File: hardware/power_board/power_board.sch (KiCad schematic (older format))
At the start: 25 parts, among them J1 Barrel_Jack, J2 Conn_01x05_Male, U1 LM1117-ADJ, U2 LM1117-ADJ, U3 LM1117-ADJ, U4 LM2776

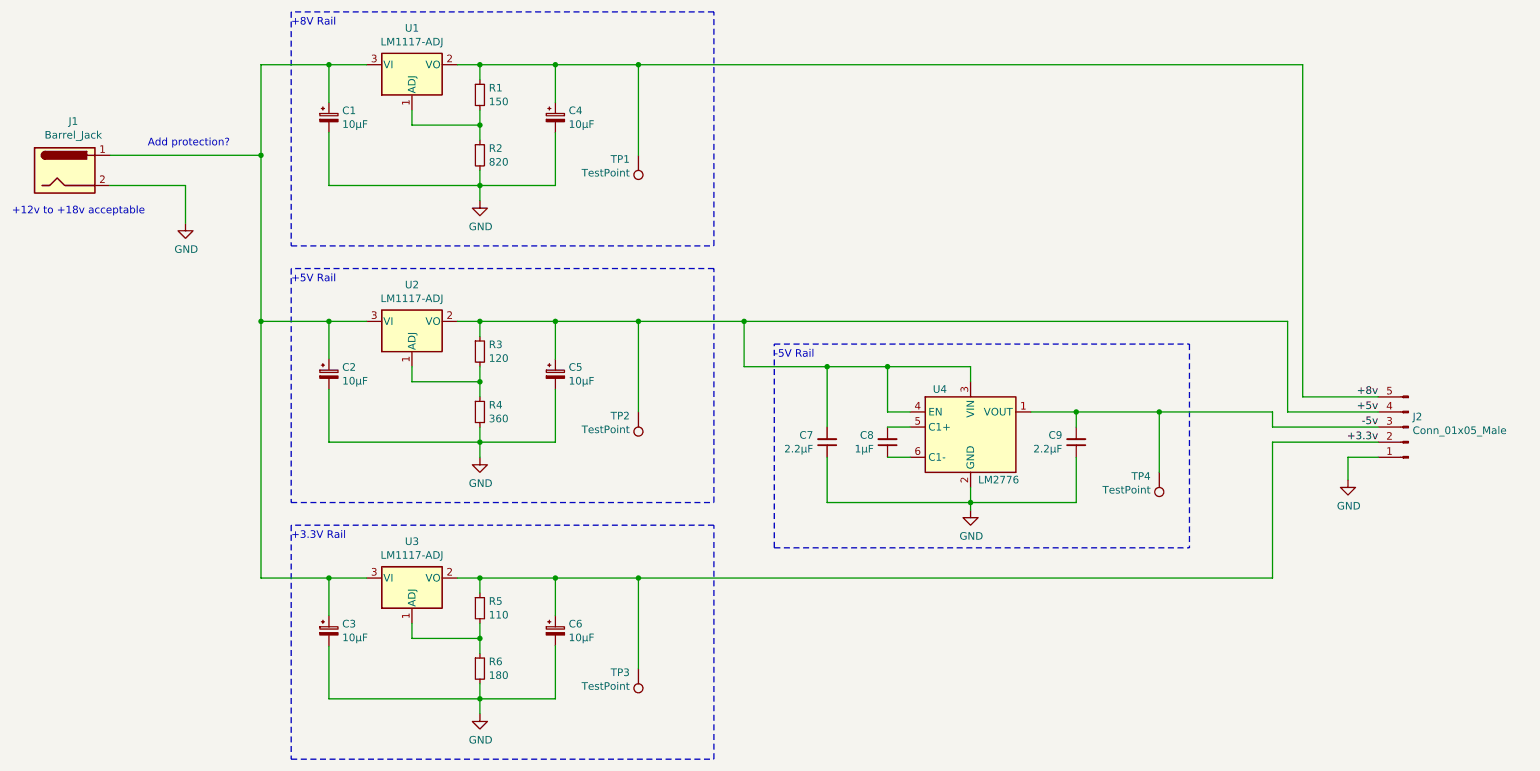
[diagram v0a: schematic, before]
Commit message: Made the board design a little more spacious
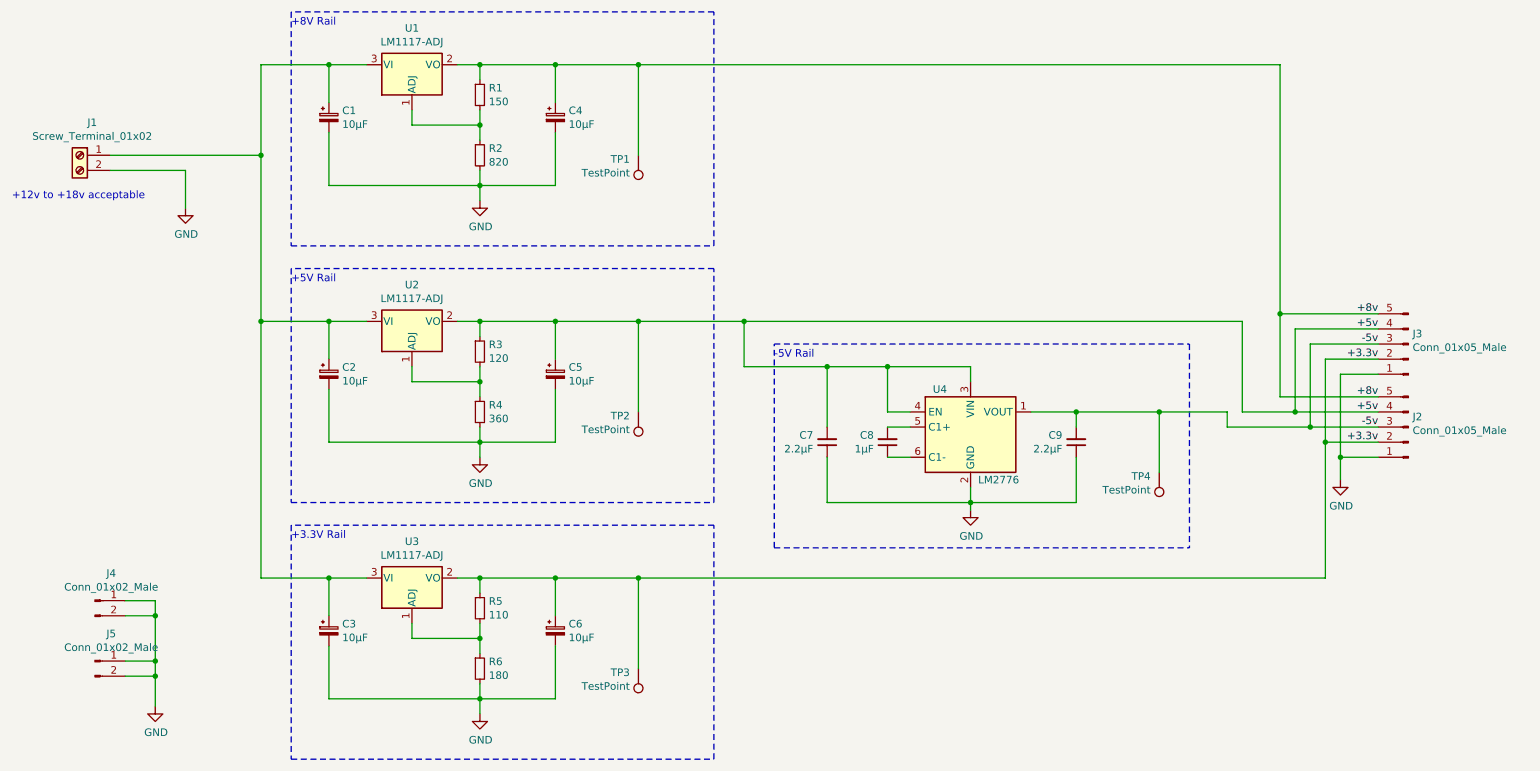
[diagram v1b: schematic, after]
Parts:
- removed J1: Barrel_Jack, Connector_BarrelJack:BarrelJack_CUI_PJ-063AH_Horizontal, symbol Connector:Barrel_Jack
- added J1: Screw_Terminal_01x02, TerminalBlock_Phoenix:TerminalBlock_Phoenix_PT-1,5-2-5.0-H_1x02_P5.00mm_Horizontal, symbol Connector:Screw_Terminal_01x02
- added J3: Conn_01x05_Male, Connector_PinHeader_2.54mm:PinHeader_1x05_P2.54mm_Vertical, symbol Connector:Conn_01x05_Male
- added J4, J5: Conn_01x02_Male, Connector_PinHeader_2.54mm:PinHeader_1x02_P2.54mm_Vertical, symbol Connector:Conn_01x02_Male
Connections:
- net +3.3v: now also J3.2 (Pin_2)
- net +5v: now also J3.4 (Pin_4)
- net +8v: now also J3.5 (Pin_5)
- net -5v: now also J3.3 (Pin_3)
- net GND: now also J1.2 (Pin_2), J3.1 (Pin_1), J4.1 (Pin_1), J4.2 (Pin_2), J5.1 (Pin_1), J5.2 (Pin_2)
- net at C1.1, C2.1, C3.1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: now also J1.1 (Pin_1)
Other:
- note removed: "Add protection?"
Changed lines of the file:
@@
 $EndDescr
-$Comp
-L Connector:Barrel_Jack J1
-U 1 1 5E18CE6A
-P 1450 2300
-F 0 "J1" H 1507 2625 50  0000 C CNN
-F 1 "Barrel_Jack" H 1507 2534 50  0000 C CNN
-F 2 "Connector_BarrelJack:BarrelJack_CUI_PJ-063AH_Horizontal" H 1500 2260 50  0001 C CNN
-F 3 "https://us.schurter.com/bundles/snceschurter/epim/_ProdPool_/newDS/en/typ_4840.2201.pdf" H 1500 2260 50  0001 C CNN
-F 4 "486-3381-ND" H 1450 2300 50  0001 C CNN "Digikey"
-	1    1450 2300
-	1    0    0    -1
-$EndComp
-$Comp
-L power:GND #PWR01
-U 1 1 5E19C530
-P 2250 2650
-F 0 "#PWR01" H 2250 2400 50  0001 C CNN
-F 1 "GND" H 2255 2477 50  0000 C CNN
-F 2 "" H 2250 2650 50  0001 C CNN
-F 3 "" H 2250 2650 50  0001 C CNN
-	1    2250 2650
-	1    0    0    -1
-$EndComp
-Wire Wire Line
-	2250 2400 2250 2650
 $Comp
 L Regulator_Linear:LM1117-ADJ U2
@@
 $EndComp
 Wire Wire Line
-	9450 5000 9450 4100
-Wire Wire Line
-	9450 4100 10150 4100
-Wire Wire Line
-	9450 4000 10150 4000
-Wire Wire Line
 	8150 3900 8700 3900
-Wire Wire Line
-	9550 3300 9550 3900
-Wire Wire Line
-	9550 3900 10150 3900
-Wire Wire Line
-	9650 1600 9650 3800
-Wire Wire Line
-	9650 3800 10150 3800
-Wire Wire Line
-	9450 3900 9450 4000
 $Comp
 L power:GND #PWR06
 U 1 1 5E251D94
-P 9950 4350
-F 0 "#PWR06" H 9950 4100 50  0001 C CNN
-F 1 "GND" H 9955 4177 50  0000 C CNN
-F 2 "" H 9950 4350 50  0001 C CNN
-F 3 "" H 9950 4350 50  0001 C CNN
-	1    9950 4350
-	1    0    0    -1
-$EndComp
-Wire Wire Line
-	9950 4350 9950 4200
-Wire Wire Line
-	9950 4200 10150 4200
-Text Notes 1100 2600 0    50   ~ 0
+P 9900 4350
+F 0 "#PWR06" H 9900 4100 50  0001 C CNN
+F 1 "GND" H 9905 4177 50  0000 C CNN
+F 2 "" H 9900 4350 50  0001 C CNN
+F 3 "" H 9900 4350 50  0001 C CNN
+	1    9900 4350
+	1    0    0    -1
+$EndComp
+Text Notes 1100 2500 0    50   ~ 0
 +12v to +18v acceptable
-Wire Wire Line
-	1750 2400 2250 2400
 Wire Wire Line
 	4700 1600 5250 1600
@@
 Connection ~ 5250 1600
 Wire Wire Line
-	5250 1600 9650 1600
+	5250 1600 9500 1600
 Connection ~ 5250 3300
 Connection ~ 5250 5000
 Wire Wire Line
-	5250 5000 9450 5000
-Wire Wire Line
 	5250 3300 5950 3300
 Wire Wire Line
@@
 	5950 3600 5950 3300
 Connection ~ 6500 3600
-Connection ~ 5950 3300
-Wire Wire Line
-	5950 3300 9550 3300
 Wire Wire Line
 	6900 4000 7050 4000
@@
 Wire Wire Line
 	8700 4300 8700 3900
-Connection ~ 8700 3900
-Wire Wire Line
-	8700 3900 9450 3900
 Wire Notes Line
 	8900 3450 8900 4800
@@
 Wire Notes Line
 	6150 3450 8900 3450
-Wire Wire Line
-	1750 2200 2750 2200
-Text Notes 2000 2150 0    50   ~ 0
-Add protection?
 $Comp
 L Device:CP_Small C4
@@
 Wire Wire Line
 	3200 5000 3450 5000
+Wire Wire Line
+	1750 2200 2750 2200
+$Comp
+L Connector:Screw_Terminal_01x02 J1
+U 1 1 5E310E8A
+P 1550 2200
+F 0 "J1" H 1468 2417 50  0000 C CNN
+F 1 "Screw_Terminal_01x02" H 1468 2326 50  0000 C CNN
+F 2 "TerminalBlock_Phoenix:TerminalBlock_Phoenix_PT-1,5-2-5.0-H_1x02_P5.00mm_Horizontal" H 1550 2200 50  0001 C CNN
+F 3 "~" H 1550 2200 50  0001 C CNN
+	1    1550 2200
+	-1   0    0    -1
+$EndComp
+Wire Wire Line
+	1750 2300 2250 2300
+Wire Wire Line
+	2250 2300 2250 2550
+$Comp
+L power:GND #PWR01
+U 1 1 5E19C530
+P 2250 2550
+F 0 "#PWR01" H 2250 2300 50  0001 C CNN
+F 1 "GND" H 2255 2377 50  0000 C CNN
+F 2 "" H 2250 2550 50  0001 C CNN
+F 3 "" H 2250 2550 50  0001 C CNN
+	1    2250 2550
+	1    0    0    -1
+$EndComp
+$Comp
+L Connector:Conn_01x05_Male J3
+U 1 1 5E323659
+P 10350 3450
+F 0 "J3" H 10322 3382 50  0000 R CNN
+F 1 "Conn_01x05_Male" H 10322 3473 50  0000 R CNN
+F 2 "Connector_PinHeader_2.54mm:PinHeader_1x05_P2.54mm_Vertical" H 10350 3450 50  0001 C CNN
+F 3 "~" H 10350 3450 50  0001 C CNN
+	1    10350 3450
+	-1   0    0    1
+$EndComp
+Text Label 10150 3550 2    50   ~ 0
++3.3v
+Text Label 10150 3450 2    50   ~ 0
+-5v
+Text Label 10150 3350 2    50   ~ 0
++5v
+Text Label 10150 3250 2    50   ~ 0
++8v
+Wire Wire Line
+	10150 3650 9900 3650
+Wire Wire Line
+	9900 3650 9900 4200
+Wire Wire Line
+	9900 4200 10150 4200
+Wire Wire Line
+	10150 4100 9800 4100
+Wire Wire Line
+	9800 4100 9800 3550
+Wire Wire Line
+	9800 3550 10150 3550
+Wire Wire Line
+	10150 4000 9700 4000
+Wire Wire Line
+	9700 4000 9700 3450
+Wire Wire Line
+	9700 3450 10150 3450
+Wire Wire Line
+	10150 3900 9600 3900
+Wire Wire Line
+	9600 3900 9600 3350
+Wire Wire Line
+	9600 3350 10150 3350
+Wire Wire Line
+	10150 3800 9500 3800
+Wire Wire Line
+	9500 3800 9500 3250
+Wire Wire Line
+	9500 3250 10150 3250
+Wire Wire Line
+	9500 3250 9500 1600
+Connection ~ 9500 3250
+Wire Wire Line
+	9800 4100 9800 5000
+Wire Wire Line
+	5250 5000 9800 5000
+Connection ~ 9800 4100
+Wire Wire Line
+	9700 4000 9150 4000
+Wire Wire Line
+	9150 4000 9150 3900
+Wire Wire Line
+	9150 3900 8700 3900
+Connection ~ 9700 4000
+Connection ~ 8700 3900
+Wire Wire Line
+	5950 3300 9250 3300
+Wire Wire Line
+	9250 3300 9250 3900
+Wire Wire Line
+	9250 3900 9600 3900
+Connection ~ 5950 3300
+Connection ~ 9600 3900
+Wire Wire Line
+	9900 4350 9900 4200
+Connection ~ 9900 4200
+$Comp
+L Connector:Conn_01x02_Male J4
+U 1 1 5E38A7BA
+P 1650 5150
+F 0 "J4" H 1758 5331 50  0000 C CNN
+F 1 "Conn_01x02_Male" H 1758 5240 50  0000 C CNN
+F 2 "Connector_PinHeader_2.54mm:PinHeader_1x02_P2.54mm_Vertical" H 1650 5150 50  0001 C CNN
+F 3 "~" H 1650 5150 50  0001 C CNN
+	1    1650 5150
+	1    0    0    -1
+$EndComp
+$Comp
+L Connector:Conn_01x02_Male J5
+U 1 1 5E38D05F
+P 1650 5550
+F 0 "J5" H 1758 5731 50  0000 C CNN
+F 1 "Conn_01x02_Male" H 1758 5640 50  0000 C CNN
+F 2 "Connector_PinHeader_2.54mm:PinHeader_1x02_P2.54mm_Vertical" H 1650 5550 50  0001 C CNN
+F 3 "~" H 1650 5550 50  0001 C CNN
+	1    1650 5550
+	1    0    0    -1
+$EndComp
+$Comp
+L power:GND #PWR07
+U 1 1 5E38D67A
+P 2050 5850
+F 0 "#PWR07" H 2050 5600 50  0001 C CNN
+F 1 "GND" H 2055 5677 50  0000 C CNN
+F 2 "" H 2050 5850 50  0001 C CNN
+F 3 "" H 2050 5850 50  0001 C CNN
+	1    2050 5850
+	1    0    0    -1
+$EndComp
+Wire Wire Line
+	1850 5650 2050 5650
+Wire Wire Line
+	2050 5650 2050 5850
+Wire Wire Line
+	1850 5550 2050 5550
+Wire Wire Line
+	2050 5550 2050 5650
+Connection ~ 2050 5650
+Wire Wire Line
+	1850 5250 2050 5250
+Wire Wire Line
+	2050 5250 2050 5550
+Connection ~ 2050 5550
+Wire Wire Line
+	1850 5150 2050 5150
+Wire Wire Line
+	2050 5150 2050 5250
+Connection ~ 2050 5250
 $EndSCHEMATC
